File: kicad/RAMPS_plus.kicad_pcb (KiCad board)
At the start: 2 copper layers, 122 x 68 mm, 135 parts, among them CON1 CON10, CON10 Stepstick_Left_Connector, CON11 Stepstick_Right_Connector, CON12 Stepstick_Left_Connector, CON13 Stepstick_Right_Connector, CON14 Stepstick_Left_Connector, CON15 Stepstick_Right_Connector, CON16 CON14x2, CON17 Stepstick_Left_Connector, CON18 Stepstick_Right_Connector, CON19 Stepstick_Left_Connector, CON2 CON8, CON20 Stepstick_Right_Connector, CON21 Panel1, CON22 Panel2, CON23 PS-ON, CON24 CON6, CON25 FAN, CON26 Chamber, CON27 BED, CON28 BED_Th, CON3 CON8, CON4 CON8, CON5 AUX, CON6 CON8, CON7 CON8, CON8 CON18x2, CON9 Carriage, Q1 IRLR2905ZPBF, Q2 IRLR2905ZPBF, Q3 FDC6401N, Q4 FDC6401N, Q5 IRLR2905ZPBF, Q6 FDC6401N, Q7 FDC6401N, Q8 FDC6401N, Q9 FDC6401N, SW1 RESET, U1 CD4504BPW, U2 SN74HCT245PW

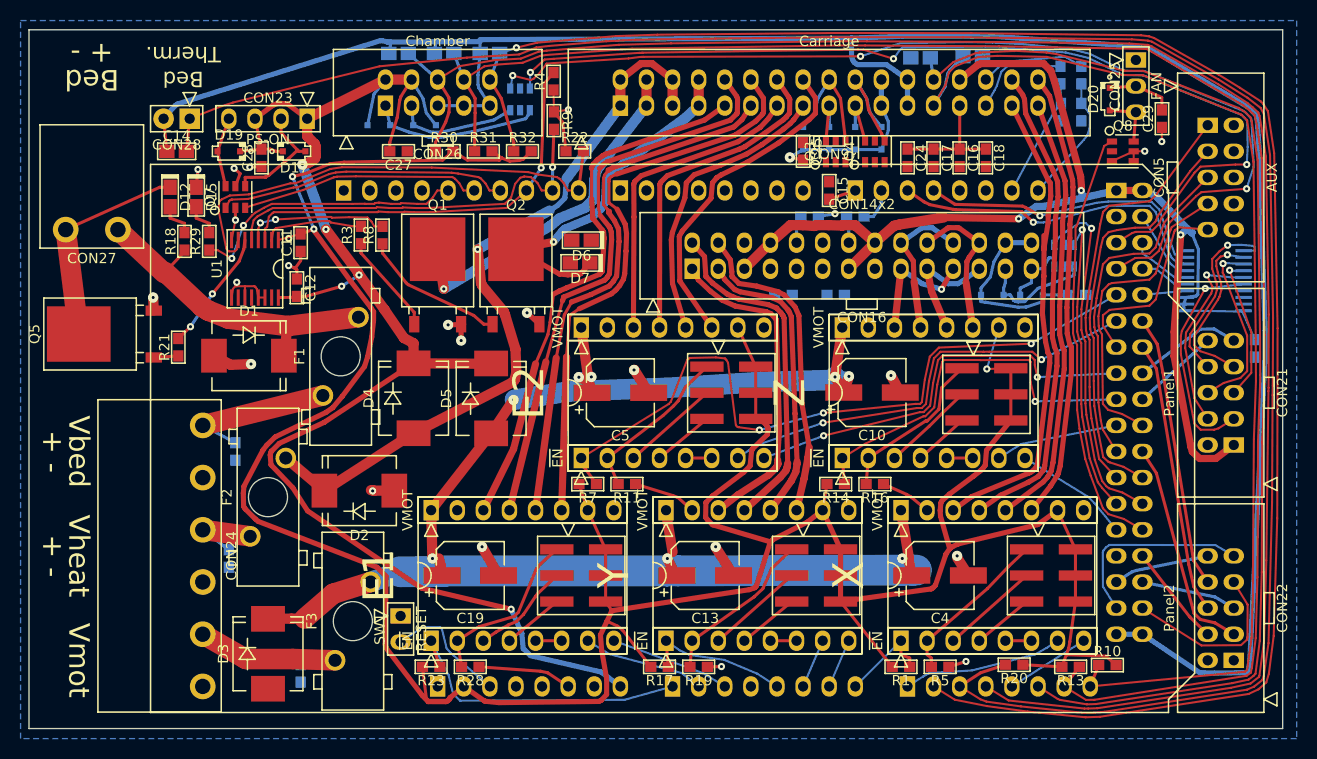
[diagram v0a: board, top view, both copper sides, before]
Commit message: Pin swap. Route.
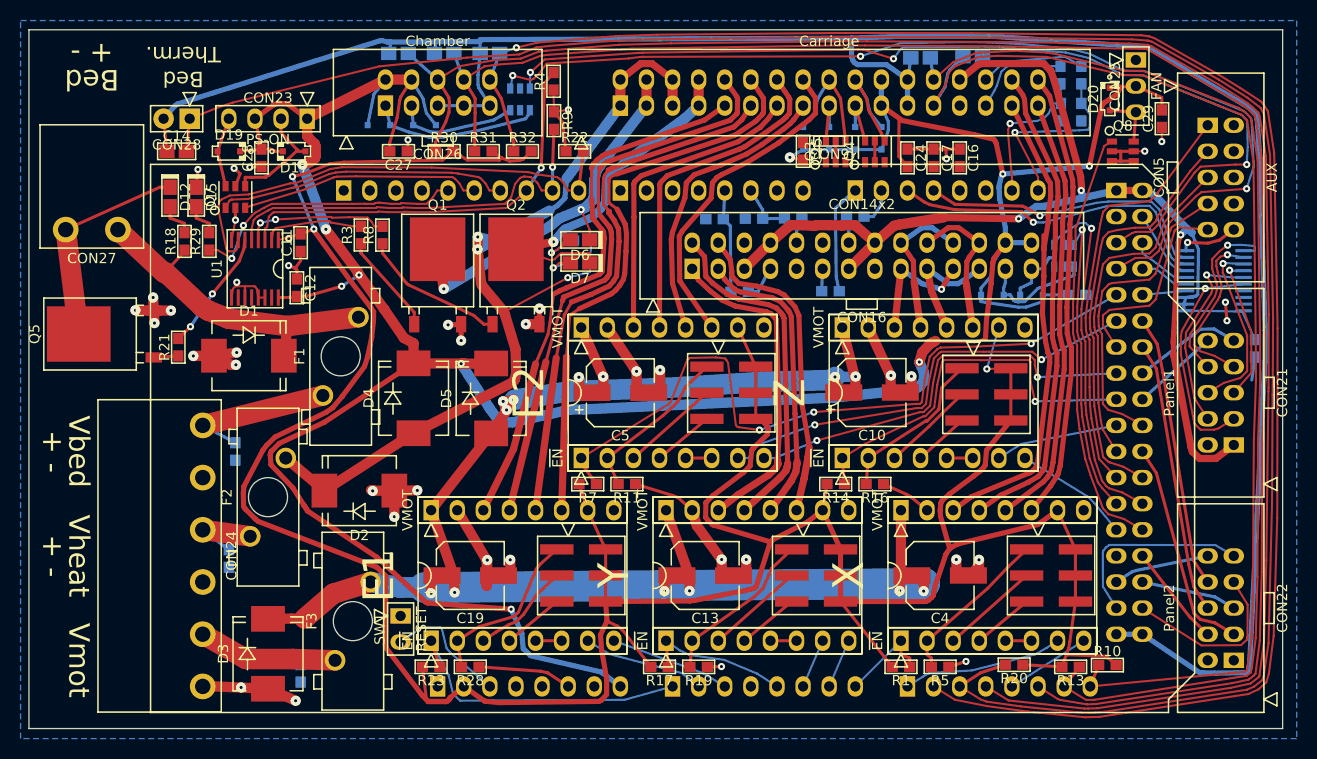
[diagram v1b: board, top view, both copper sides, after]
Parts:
- C15, C18: moved to B.Cu
- moved C18 23.3 mm to (95.6, 43.4), turned to 0 degrees
- moved C15 11.5 mm to (91.7, 43.4), turned to 0 degrees
- moved R24 4.28 mm to (94.2, 50.5), turned to 180 degrees
- moved R6 2.30 mm to (78.7, 47.8)
- moved R2 2.18 mm to (78.8, 45.5)
- moved R27 1.61 mm to (99.4, 43.4), turned to 180 degrees
- moved R25 0.62 mm to (103.0, 50.4)
- moved D6 0.16 mm to (78.6, 45.4)
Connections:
- C15 pad 1: D2 -> D3
- C17 pad 1: D25 -> D15
- C18 pad 1: D3 -> D2
- CON7 pad 2: (no net) -> D15
- R24 pad 1: D2 -> D3
- R26 pad 1: D25 -> D15
- R27 pad 1: D3 -> D2
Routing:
- net +12V: track 191.9 -> 305.8 mm, vias 6 -> 10
- net GND: track 92.2 -> 175.8 mm, vias 22 -> 40
- net Vmot: track 155.4 -> 194.2 mm, vias 8 -> 13
- net Vheat: track 71.9 -> 88.3 mm, vias 1 -> 3
- net D14: track 0.00 -> 10.7 mm
- net D3: track 1.65 -> 10.3 mm, vias 1 -> 0
- net D21: track 12.5 -> 18.1 mm, vias 0 -> 1
- net Net-(D6-Pad1): track 0.00 -> 4.89 mm, vias 0 -> 1
- net Net-(D7-Pad1): track 0.00 -> 3.78 mm, vias 0 -> 1
- net D25: track 9.75 -> 6.06 mm
- net D15: track 0.00 -> 3.68 mm
- net /YZ axis/Ymin: track 0.00 -> 3.51 mm
- net /Carriage/heater1: track 34.3 -> 37.5 mm, vias 1 -> 2
- net D20: track 11.6 -> 14.3 mm, vias 0 -> 1
- net D2: track 2.68 -> 5.21 mm
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
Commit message: Route.
Routed board with some minor DRC issues.
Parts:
- removed C24: 100n/50V, pnRLC:0603
- moved C16 2.58 mm to (113.0, 37.2)
- moved C17 2.25 mm to (110.8, 37.2)
- moved C25 1.52 mm to (98.9, 37.2)
- moved Q3 1.16 mm to (102.4, 37.3), turned to 270 degrees
- moved Q4 0.52 mm to (107.0, 37.2), turned to 270 degrees
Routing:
- net D6: track 0.00 -> 23.1 mm, vias 0 -> 1
- net GND: track 175.8 -> 198.6 mm, vias 40 -> 45
- net D7: track 0.00 -> 21.4 mm, vias 0 -> 1
- net D4: track 0.00 -> 17.7 mm, vias 0 -> 1
- net D5: track 0.00 -> 15.0 mm, vias 0 -> 1
- net AGND: track 208.2 -> 222.1 mm
- net D14: track 10.7 -> 20.7 mm
- net D15: track 3.68 -> 9.22 mm
- net /Carriage/OC4: track 12.0 -> 15.6 mm
- net /Carriage/OC2: track 11.6 -> 14.9 mm
- net +12V: track 305.8 -> 303.2 mm
- net (no net): track 1.89 -> 0.00 mm, vias 2 -> 0
- net D24: track 94.4 -> 96.2 mm
- net /Carriage/OC3: track 5.59 -> 7.39 mm
- net D26: track 99.0 -> 100.7 mm
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
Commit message: Fix DRC issues.
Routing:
- net /Carriage/XmotorA: track 46.8 -> 45.6 mm

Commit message: Route. Generate gerber.
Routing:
- net GND: track 198.6 -> 219.5 mm
- net (no net): track 0.00 -> 2.70 mm
- net D38: track 12.0 -> 13.7 mm
- added copper zone on F.Cu, net /YZ axis/BED
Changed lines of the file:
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@@
     (thickness 1.6)
     (drawings 12)
-    (tracks 2450)
+    (tracks 2471)
     (zones 0)
     (modules 134)
@@
     (15 F.Cu signal)
     (0 B.Cu signal)
-    (16 B.Adhes user)
-    (17 F.Adhes user)
-    (18 B.Paste user)
-    (19 F.Paste user)
-    (20 B.SilkS user)
-    (21 F.SilkS user)
-    (22 B.Mask user)
-    (23 F.Mask user)
+    (16 B.Adhes user hide)
+    (17 F.Adhes user hide)
+    (18 B.Paste user hide)
+    (19 F.Paste user hide)
+    (20 B.SilkS user hide)
+    (21 F.SilkS user hide)
+    (22 B.Mask user hide)
+    (23 F.Mask user hide)
     (24 Dwgs.User user)
     (25 Cmts.User user)
@@
   )
   (setup
-    (last_trace_width 0.16)
+    (last_trace_width 0.2)
     (user_trace_width 0.16)
     (user_trace_width 0.2)
@@
     (pad_to_mask_clearance 0)
     (aux_axis_origin 0 0)
-    (visible_elements 7FFFFF7F)
+    (visible_elements 7FFFFF1F)
     (pcbplotparams
-      (layerselection 3178497)
+      (layerselection 284196865)
       (usegerberextensions true)
       (excludeedgelayer true)
@@
       (psnegative false)
       (psa4output false)
-      (plotreference true)
-      (plotvalue true)
+      (plotreference false)
+      (plotvalue false)
       (plotinvisibletext false)
       (padsonsilk false)
-      (subtractmaskfromsilk false)
+      (subtractmaskfromsilk true)
       (outputformat 1)
       (mirror false)
-      (drillshape 1)
+      (drillshape 0)
       (scaleselection 1)
-      (outputdirectory ""))
+      (outputdirectory gerber))
   )
   (net 0 "")
@@
     (effects (font (size 2 2) (thickness 0.3)))
   )
+  (segment (start 71.6788 31.7754) (end 74.3458 31.7754) (width 0.2) (layer B.Cu) (net 0))
+  (segment (start 74.3458 31.7754) (end 74.3712 31.8008) (width 0.2) (layer B.Cu) (net 0))
   (via (at 128.191 38.2685) (size 0.7) (layers F.Cu B.Cu) (net 1))
   (via (at 119.767 39.0408) (size 0.7) (layers F.Cu B.Cu) (net 1))
@@
   (segment (start 143.493 40.4737) (end 144.1854 38.2825) (width 0.2) (layer B.Cu) (net 15))
   (via (at 122.528 55.5473) (size 0.7) (layers F.Cu B.Cu) (net 16))
-  (via (at 101.376 62.209) (size 0.7) (layers F.Cu B.Cu) (net 16))
+  (via (at 101.5238 63.6524) (size 0.7) (layers F.Cu B.Cu) (net 16))
   (via (at 96.081 63.9524) (size 0.7) (layers F.Cu B.Cu) (net 16))
   (segment (start 117.196 55.8277) (end 122.528 55.5473) (width 0.2) (layer F.Cu) (net 16))
@@
   (segment (start 111.715 61.4068) (end 111.883 61.2381) (width 0.2) (layer F.Cu) (net 16))
   (segment (start 111.27 61.4068) (end 111.715 61.4068) (width 0.2) (layer F.Cu) (net 16))
-  (segment (start 101.376 62.209) (end 111.27 61.4068) (width 0.2) (layer F.Cu) (net 16))
-  (segment (start 96.081 63.9524) (end 101.376 62.209) (width 0.2) (layer B.Cu) (net 16))
+  (segment (start 101.5238 63.6524) (end 111.27 61.4068) (width 0.2) (layer F.Cu) (net 16))
+  (segment (start 96.081 63.9524) (end 101.5238 63.6524) (width 0.2) (layer B.Cu) (net 16))
   (segment (start 94.0678 63.6774) (end 96.081 63.9524) (width 0.2) (layer F.Cu) (net 16))
   (segment (start 93.9585 63.6577) (end 94.0678 63.6774) (width 0.2) (layer F.Cu) (net 16))
@@
   (segment (start 78.742 67.1867) (end 80.225 69.215) (width 0.3) (layer F.Cu) (net 16))
   (via (at 123.53 57.098) (size 0.7) (layers F.Cu B.Cu) (net 17))
-  (via (at 101.469 63.4477) (size 0.7) (layers F.Cu B.Cu) (net 17))
+  (via (at 102.4382 64.2874) (size 0.7) (layers F.Cu B.Cu) (net 17))
   (segment (start 122.63 56.3304) (end 123.53 57.098) (width 0.2) (layer F.Cu) (net 17))
   (segment (start 118.46 56.3304) (end 122.63 56.3304) (width 0.2) (layer F.Cu) (net 17))
@@
   (segment (start 111.882 61.8103) (end 112.287 61.4052) (width 0.2) (layer F.Cu) (net 17))
   (segment (start 111.408 61.8103) (end 111.882 61.8103) (width 0.2) (layer F.Cu) (net 17))
-  (segment (start 101.469 63.4477) (end 111.408 61.8103) (width 0.2) (layer F.Cu) (net 17))
-  (segment (start 96.3236 65.253) (end 101.469 63.4477) (width 0.2) (layer B.Cu) (net 17))
+  (segment (start 102.4382 64.2874) (end 111.408 61.8103) (width 0.2) (layer F.Cu) (net 17))
+  (segment (start 96.3236 65.253) (end 102.4382 64.2874) (width 0.2) (layer B.Cu) (net 17))
   (segment (start 95.8712 65.4857) (end 96.3236 65.253) (width 0.2) (layer B.Cu) (net 17))
   (segment (start 95.582 65.8029) (end 95.8712 65.4857) (width 0.2) (layer B.Cu) (net 17))
@@
   (segment (start 130.81 53.34) (end 123.53 57.098) (width 0.2) (layer B.Cu) (net 17))
   (via (at 123.127 58.8063) (size 0.7) (layers F.Cu B.Cu) (net 18))
-  (via (at 101.669 64.9732) (size 0.7) (layers F.Cu B.Cu) (net 18))
+  (via (at 101.854 65.1764) (size 0.7) (layers F.Cu B.Cu) (net 18))
   (segment (start 122.877 57.6327) (end 123.127 58.8063) (width 0.2) (layer F.Cu) (net 18))
   (segment (start 122.877 57.1481) (end 122.877 57.6327) (width 0.2) (layer F.Cu) (net 18))
@@
   (segment (start 112.049 62.2138) (end 112.69 61.5723) (width 0.16) (layer F.Cu) (net 18))
   (segment (start 111.696 62.2138) (end 112.049 62.2138) (width 0.2) (layer F.Cu) (net 18))
-  (segment (start 101.669 64.9732) (end 111.696 62.2138) (width 0.2) (layer F.Cu) (net 18))
-  (segment (start 97.5735 66.675) (end 101.669 64.9732) (width 0.2) (layer B.Cu) (net 18))
+  (segment (start 101.854 65.1764) (end 111.696 62.2138) (width 0.2) (layer F.Cu) (net 18))
+  (segment (start 97.5735 66.675) (end 101.854 65.1764) (width 0.2) (layer B.Cu) (net 18))
   (segment (start 96.52 66.675) (end 97.5735 66.675) (width 0.2) (layer B.Cu) (net 18))
   (segment (start 130.805 58.42) (end 123.127 58.8063) (width 0.2) (layer B.Cu) (net 18))
@@
   (segment (start 104.355 69.215) (end 104.14 66.675) (width 0.3) (layer F.Cu) (net 19))
   (segment (start 130.81 60.96) (end 122.907 61.1681) (width 0.2) (layer B.Cu) (net 19))
-  (segment (start 121.558 65.3075) (end 119.38 66.675) (width 0.2) (layer B.Cu) (net 20))
-  (segment (start 130.81 63.5) (end 121.558 65.3075) (width 0.2) (layer B.Cu) (net 20))
+  (segment (start 130.81 63.5) (end 121.0056 63.5) (width 0.2) (layer B.Cu) (net 20) (status 400000))
+  (segment (start 119.3546 65.151) (end 119.3546 66.7004) (width 0.2) (layer B.Cu) (net 20) (status 800000))
+  (segment (start 121.0056 63.5) (end 119.3546 65.151) (width 0.2) (layer B.Cu) (net 20))
+  (segment (start 119.3546 66.7004) (end 119.38 66.675) (width 0.2) (layer B.Cu) (net 20) (status C00000))
   (segment (start 128.688 71.0686) (end 130.81 73.66) (width 0.2) (layer B.Cu) (net 21))
   (segment (start 128.071 70.4515) (end 128.688 71.0686) (width 0.16) (layer B.Cu) (net 21))
@@
   (segment (start 75.946 39.2865) (end 75.9532 38.926) (width 0.3) (layer B.Cu) (net 23))
   (segment (start 75.946 40.64) (end 75.946 39.2865) (width 0.3) (layer B.Cu) (net 23))
+  (segment (start 61.1632 82.042) (end 59.2836 82.042) (width 0.5) (layer B.Cu) (net 24))
+  (segment (start 59.2836 82.042) (end 59.182 82.1436) (width 0.5) (layer B.Cu) (net 24))
+  (segment (start 61.1632 82.042) (end 63.0174 82.042) (width 0.5) (layer B.Cu) (net 24))
+  (segment (start 63.0174 82.042) (end 63.0936 81.9658) (width 0.5) (layer B.Cu) (net 24))
+  (segment (start 80.01 88.9) (end 77.5208 88.9) (width 0.5) (layer B.Cu) (net 24))
+  (segment (start 77.5208 88.9) (end 76.2508 87.63) (width 0.5) (layer B.Cu) (net 24))
+  (segment (start 107.315 48.26) (end 108.5596 47.0154) (width 0.5) (layer B.Cu) (net 24))
+  (segment (start 107.315 48.26) (end 107.315 49.9872) (width 0.5) (layer B.Cu) (net 24))
+  (segment (start 107.315 49.9872) (end 107.3912 50.0634) (width 0.5) (layer B.Cu) (net 24))
+  (segment (start 94.615 45.72) (end 95.7834 45.72) (width 0.5) (layer B.Cu) (net 24))
+  (segment (start 95.7834 45.72) (end 95.8342 45.6692) (width 0.5) (layer B.Cu) (net 24))
+  (segment (start 102.235 45.72) (end 102.235 43.7896) (width 0.5) (layer B.Cu) (net 24))
+  (segment (start 102.235 43.7896) (end 102.2858 43.7388) (width 0.5) (layer B.Cu) (net 24))
+  (segment (start 99.695 48.26) (end 102.3112 45.6438) (width 0.5) (layer B.Cu) (net 24))
+  (segment (start 102.3112 45.6438) (end 102.235 45.72) (width 0.5) (layer B.Cu) (net 24))
+  (segment (start 99.695 48.26) (end 99.695 50.0888) (width 0.5) (layer B.Cu) (net 24))
+  (segment (start 99.695 50.0888) (end 99.7966 50.1904) (width 0.5) (layer B.Cu) (net 24))
   (segment (start 125.73 47.0662) (end 128.0922 47.0662) (width 0.3) (layer B.Cu) (net 24))
   (segment (start 128.0922 47.0662) (end 128.1176 47.0408) (width 0.3) (layer B.Cu) (net 24))
@@
       )
     )
+  )
+  (zone (net 144) (net_name "/YZ axis/BED") (layer F.Cu) (hatch edge 0.508)
+    (connect_pads thru_hole_only (clearance 0.3))
+    (min_thickness 0.2)
+    (fill yes (arc_segments 16) (thermal_gap 0.508) (thermal_bridge_width 0.25))
+    (polygon
+      (pts
+        (xy 39.5 92.5) (xy 26 92.5) (xy 26 26) (xy 36.5 26) (xy 36.5 58.5)
+        (xy 39.5 58.5)
+      )
+    )

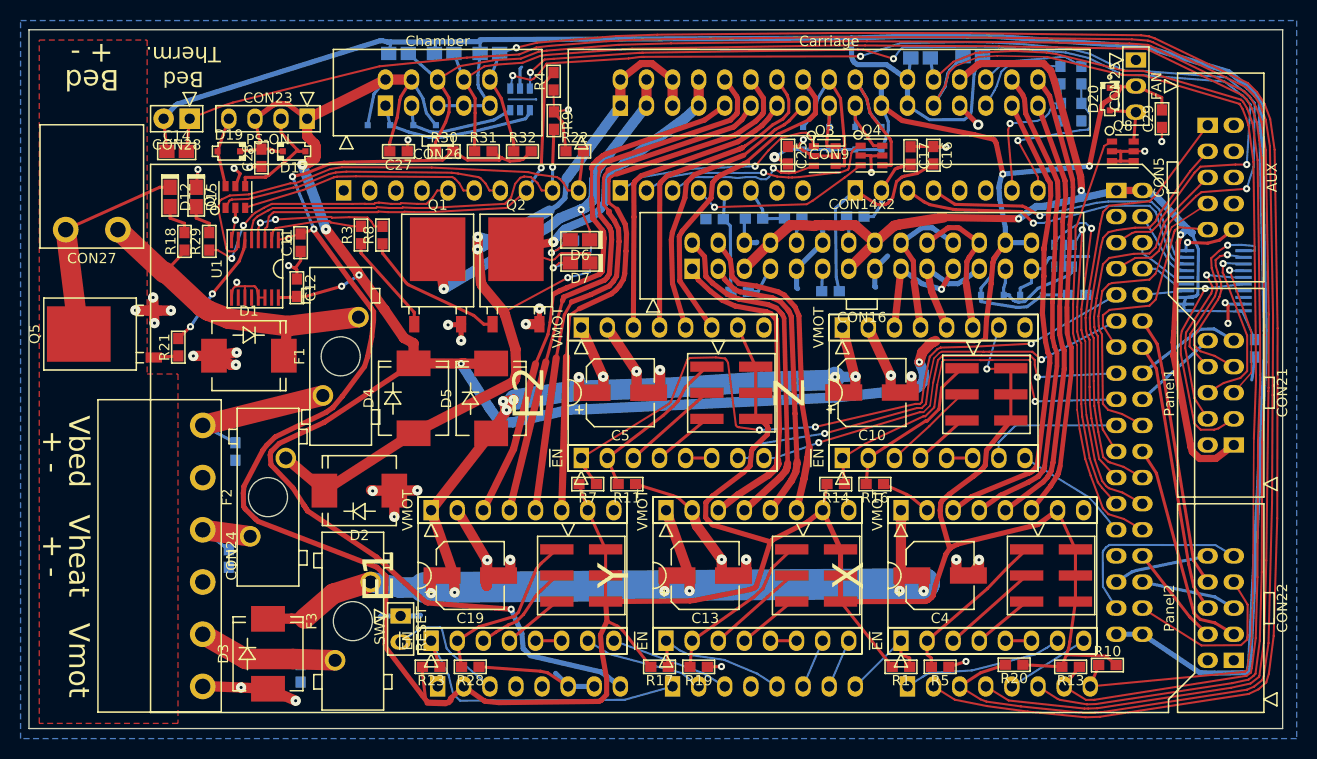
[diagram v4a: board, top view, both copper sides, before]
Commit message: Fix vias. generate gerber.
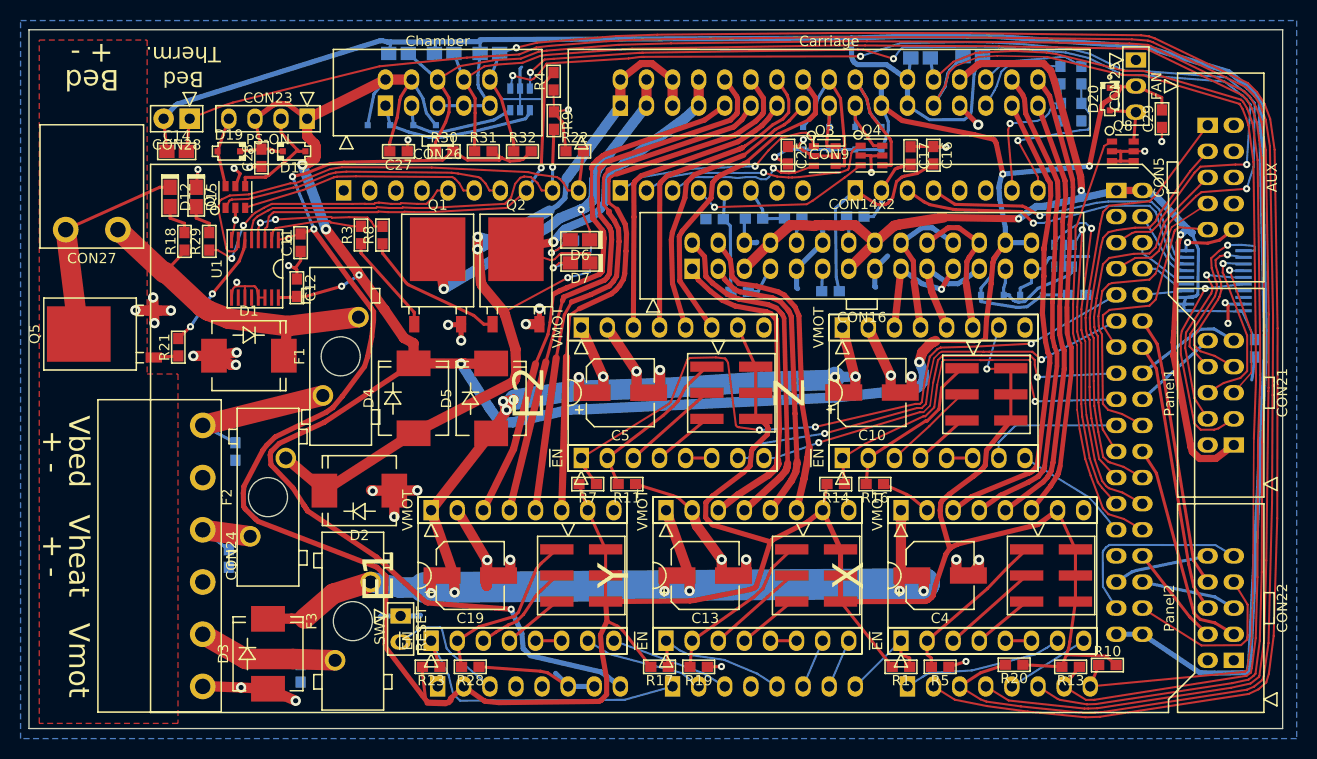
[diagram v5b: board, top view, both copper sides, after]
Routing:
- net GND: track 219.5 -> 225.4 mm
- net (no net): track 2.70 -> 0.00 mm

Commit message: Organize silkscreen.
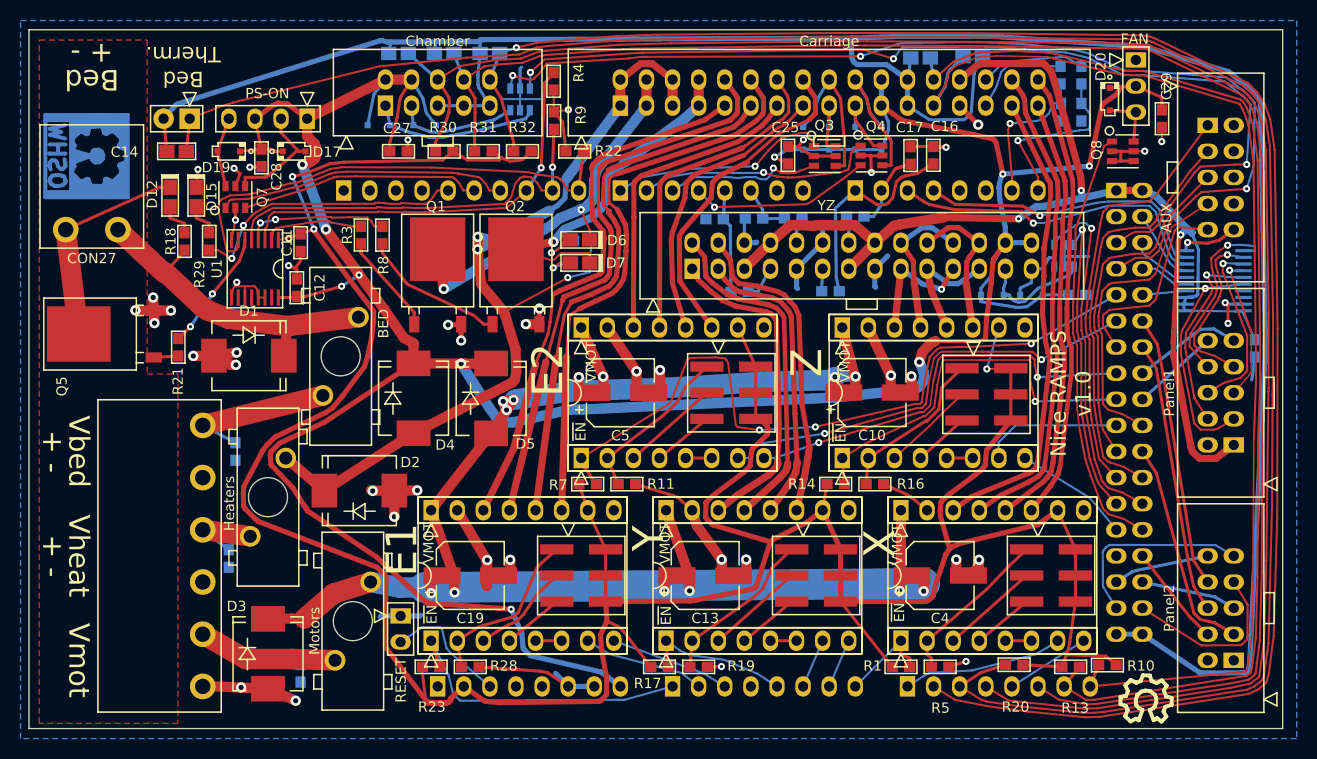
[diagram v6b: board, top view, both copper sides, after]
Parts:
- removed MECH1: ArduinoMegaShield, pnModules:ArduinoMegaShield
- added SYM: Symbol_OSHW-Logo_SilkScreen_07Jul2012, symbols:Symbol_OSHW-Logo_SilkScreen_1, F.Cu at (133.7, 90.3)
- added SYM: Symbol_OSHW-Logo_CopperTop_Negative_07Jul2012, symbols:Symbol_OSHW-Logo_CopperTop_Negative, B.Cu at (31.6, 37.3)
- CON16: value CON14x2 -> YZ
- F1: value MINI_Blade_Fuse_Holder -> BED
- F2: value MINI_Blade_Fuse_Holder -> Heaters
- F3: value MINI_Blade_Fuse_Holder -> Motors
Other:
- rule pad_to_mask_clearance: 0 -> 0.1
- board text added: "Nice RAMPS v1.0"
